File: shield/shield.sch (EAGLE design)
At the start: 13 parts, among them IC1 LM75, Q1 BUZ11BV, Q2 BUZ11BV, Q3 BUZ11BV, Q4 BUZ11BV, U1 TLC5925IDWR

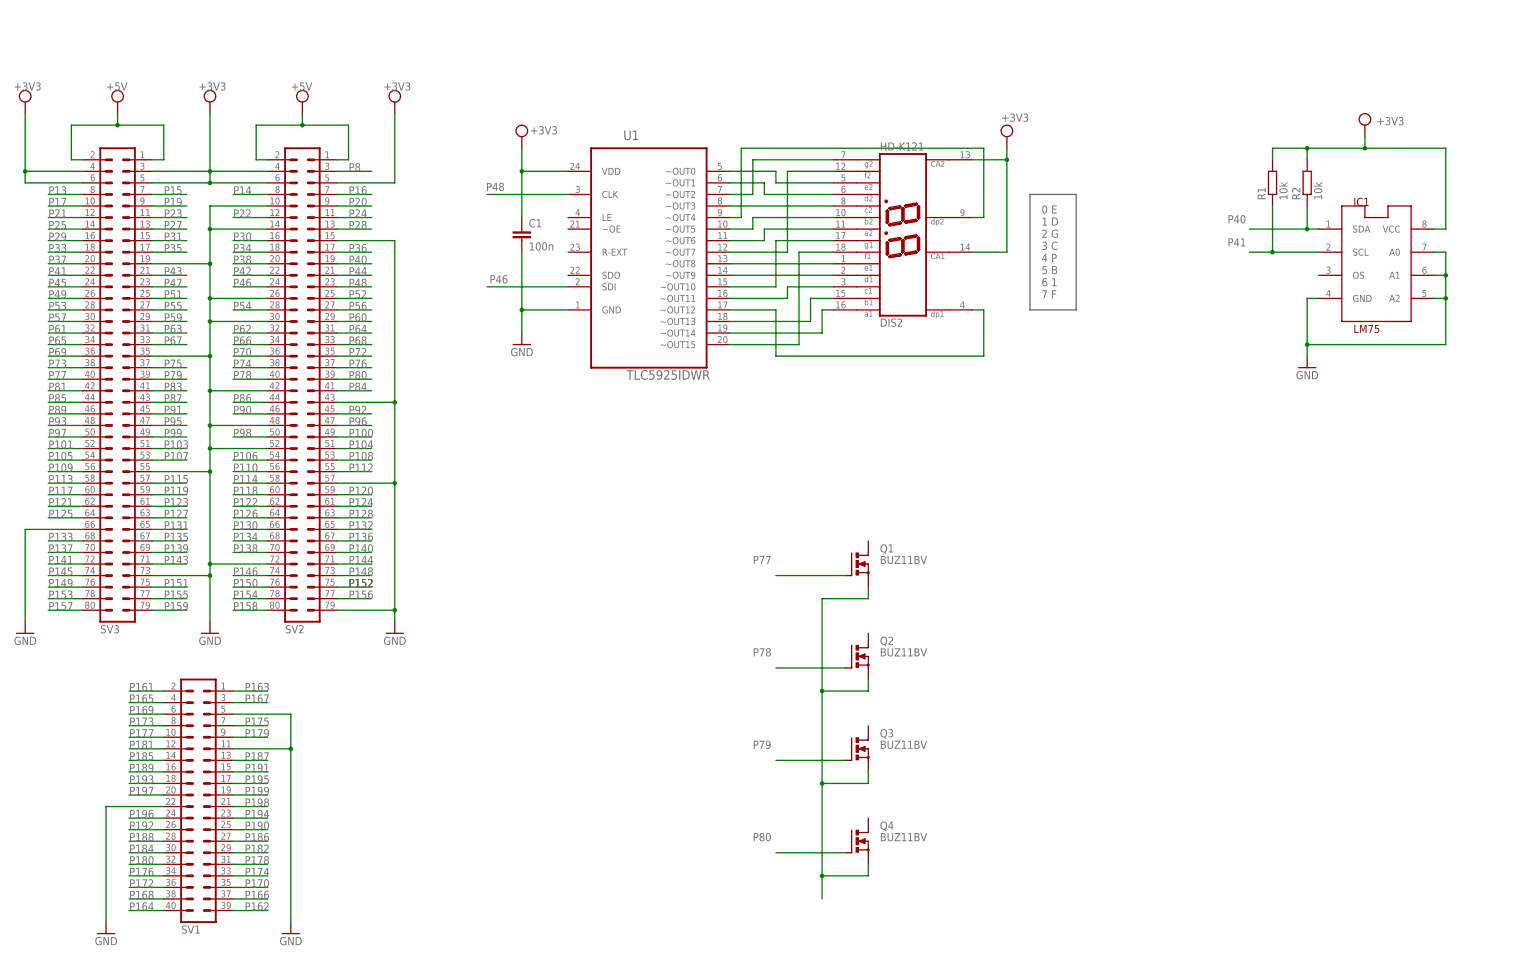
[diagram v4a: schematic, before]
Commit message: Update shield schematic and pcb
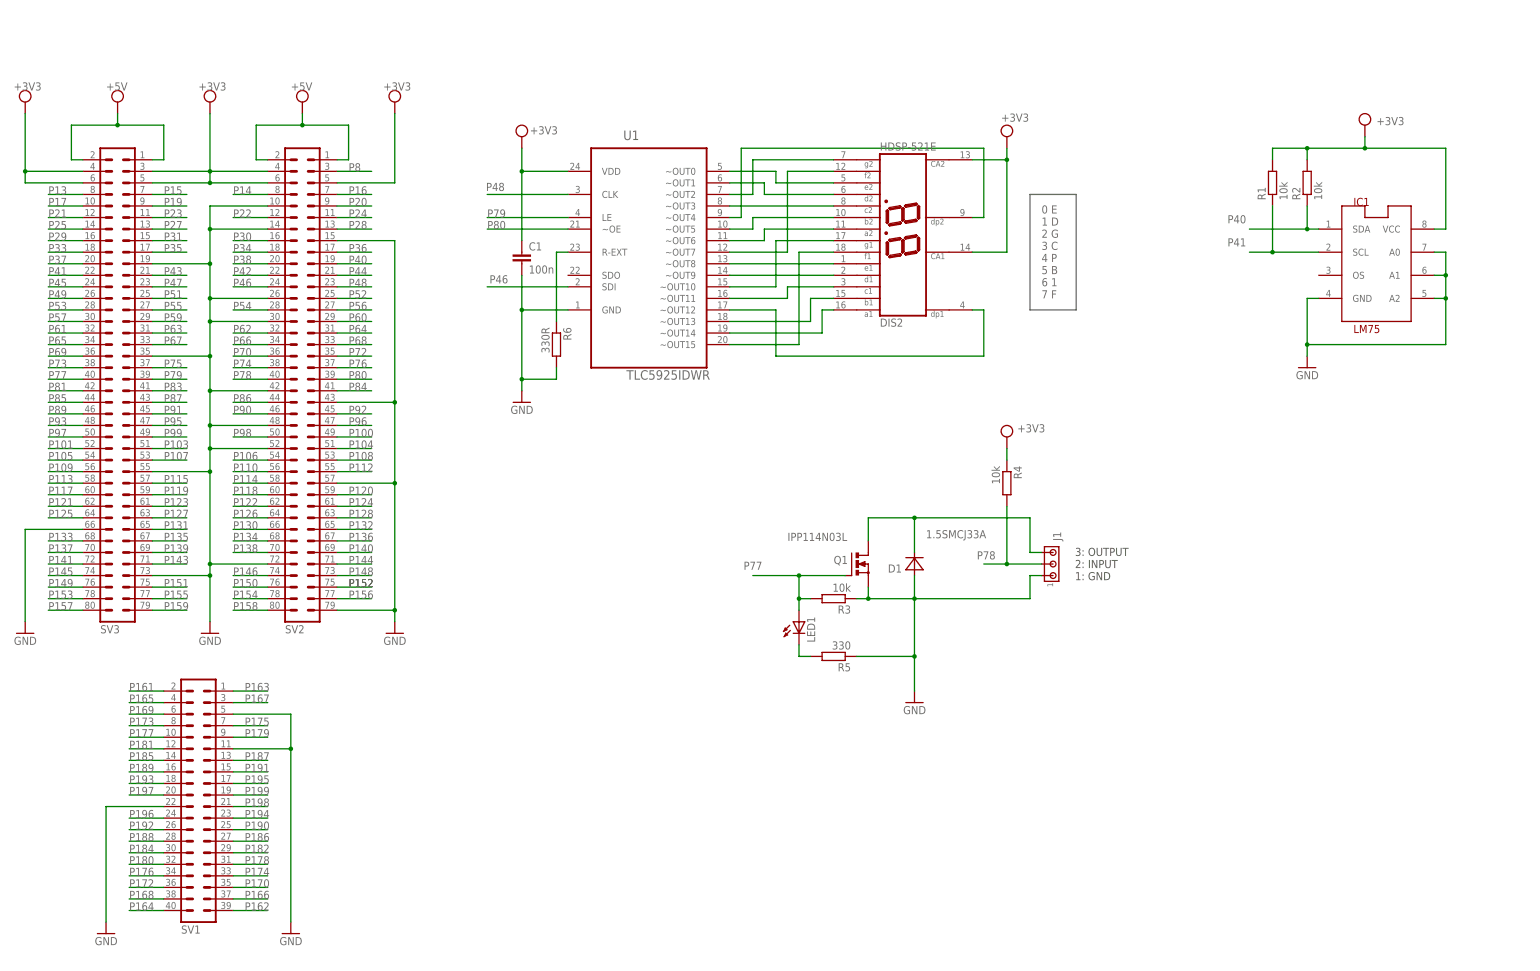
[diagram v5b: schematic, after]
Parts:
- removed Q2, Q3, Q4: BUZ11BV, transistor-power:BUZ11BV
- added D1: 1.5SMCJ33A, seb:MBRS340
- added J1: (no value), con-amp:MTA03-100
- added LED1: (no value), led:LED5MM
- added R3, R4: 10k, rcl:R-EU_0207/10
- added R5: 330, rcl:R-EU_0207/10
- added R6: 330R, rcl:R-EU_0207/10
- DIS2: value HD-K121 -> HDSP-521E
- Q1: value BUZ11BV -> IPP114N03L
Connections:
- new net N$18: LED1.C, R5.2
- new net N$20: R6.1, U1.R-EXT
- net +3V3: now also R4.1
- net GND: now also D1.A, J1.1, Q1.S, R3.1, R5.1, R6.2
- net N$17: now also D1.C, J1.3, Q1.D; no longer Q1.S, Q2.S, Q3.S, Q4.S
- net P77: now also LED1.A, R3.2
- net P78: now also J1.2, R4.2; no longer Q2.G
- net P79: now also U1.LE; no longer Q3.G
- net P80: now also U1.~OE; no longer Q4.G
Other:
- note added: "3: OUTPUT 2: INPUT 1: GND"
- moved on the sheet: C1

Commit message: Update board file
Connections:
- removed net +5V: SV2.1, SV2.2, SV3.1, SV3.2
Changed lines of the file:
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@@
 <part name="GND5" library="supply1" deviceset="GND" device=""/>
 <part name="SUPPLY2" library="supply2" deviceset="VDD" device="" value="VDD"/>
-<part name="SUPPLY1" library="supply2" deviceset="VDD" device=""/>
-<part name="SUPPLY3" library="supply2" deviceset="VDD" device=""/>
 <part name="SUPPLY4" library="supply2" deviceset="VDD" device="" value="VDD"/>
 <part name="SUPPLY5" library="supply2" deviceset="VDD" device="" value="VDD"/>
@@
 <instance part="GND5" gate="1" x="33.02" y="15.24" rot="MR0"/>
 <instance part="SUPPLY2" gate="G$1" x="-48.26" y="132.08" smashed="yes"/>
-<instance part="SUPPLY1" gate="G$1" x="-27.94" y="132.08" smashed="yes"/>
-<instance part="SUPPLY3" gate="G$1" x="12.7" y="132.08" smashed="yes"/>
 <instance part="SUPPLY4" gate="G$1" x="-7.62" y="132.08" smashed="yes"/>
 <instance part="SUPPLY5" gate="G$1" x="33.02" y="132.08" smashed="yes"/>
@@
 </segment>
 </net>
-<net name="+5V" class="0">
-<segment>
-<pinref part="SV3" gate="G$1" pin="2"/>
-<wire x1="-35.56" y1="119.38" x2="-38.1" y2="119.38" width="0.1524" layer="91"/>
-<wire x1="-38.1" y1="119.38" x2="-38.1" y2="127" width="0.1524" layer="91"/>
-<pinref part="SV3" gate="G$1" pin="1"/>
-<wire x1="-20.32" y1="119.38" x2="-17.78" y2="119.38" width="0.1524" layer="91"/>
-<wire x1="-17.78" y1="119.38" x2="-17.78" y2="127" width="0.1524" layer="91"/>
-<wire x1="-17.78" y1="127" x2="-27.94" y2="127" width="0.1524" layer="91"/>
-<pinref part="SUPPLY1" gate="G$1" pin="VDD"/>
-<wire x1="-27.94" y1="127" x2="-38.1" y2="127" width="0.1524" layer="91"/>
-<wire x1="-27.94" y1="127" x2="-27.94" y2="129.54" width="0.1524" layer="91"/>
-<label x="-30.48" y="134.62" size="1.778" layer="95"/>
-<junction x="-27.94" y="127"/>
-</segment>
-<segment>
-<wire x1="22.86" y1="119.38" x2="22.86" y2="127" width="0.1524" layer="91"/>
-<wire x1="20.32" y1="119.38" x2="22.86" y2="119.38" width="0.1524" layer="91"/>
-<pinref part="SV2" gate="G$1" pin="1"/>
-<pinref part="SV2" gate="G$1" pin="2"/>
-<wire x1="5.08" y1="119.38" x2="2.54" y2="119.38" width="0.1524" layer="91"/>
-<wire x1="2.54" y1="119.38" x2="2.54" y2="127" width="0.1524" layer="91"/>
-<wire x1="2.54" y1="127" x2="12.7" y2="127" width="0.1524" layer="91"/>
-<pinref part="SUPPLY3" gate="G$1" pin="VDD"/>
-<wire x1="12.7" y1="127" x2="22.86" y2="127" width="0.1524" layer="91"/>
-<wire x1="12.7" y1="129.54" x2="12.7" y2="127" width="0.1524" layer="91"/>
-<junction x="12.7" y="127"/>
-<label x="10.16" y="134.62" size="1.778" layer="95"/>
-</segment>
-</net>
 <net name="N$1" class="0">
 <segment>
@@
 </sheet>
 </sheets>
+<errors>
+</errors>
 </schematic>
 </drawing>

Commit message: Add capacitor
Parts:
- added C2: 100n, capacitor-wima:C2.5/2
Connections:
- net +3V3: now also C2.1
- net GND: now also C2.2
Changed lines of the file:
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@@
 <part name="R6" library="rcl" deviceset="R-EU_" device="0207/10" value="330R"/>
 <part name="D1" library="seb" deviceset="MBRS340" device="" value="1.5SMCJ33A"/>
+<part name="C2" library="capacitor-wima" deviceset="C" device="2.5/2" value="100n"/>
 </parts>
 <sheets>
@@
 <attribute name="VALUE" x="149.8346" y="36.1442" size="1.778" layer="96"/>
 </instance>
+<instance part="C2" gate="G$1" x="274.32" y="91.44"/>
 </instances>
 <busses>
@@
 <junction x="264.16" y="88.9"/>
 <junction x="233.68" y="78.74"/>
+<pinref part="C2" gate="G$1" pin="2"/>
+<wire x1="264.16" y1="78.74" x2="274.32" y2="78.74" width="0.1524" layer="91"/>
+<wire x1="274.32" y1="78.74" x2="274.32" y2="86.36" width="0.1524" layer="91"/>
+<junction x="264.16" y="78.74"/>
 </segment>
 <segment>
@@
 <wire x1="264.16" y1="104.14" x2="261.62" y2="104.14" width="0.1524" layer="91"/>
 <junction x="233.68" y="121.92"/>
-</segment>
-<segment>
+<pinref part="C2" gate="G$1" pin="1"/>
+<wire x1="264.16" y1="104.14" x2="274.32" y2="104.14" width="0.1524" layer="91"/>
+<wire x1="274.32" y1="104.14" x2="274.32" y2="93.98" width="0.1524" layer="91"/>
+<junction x="264.16" y="104.14"/>
+</segment>
+<segment>

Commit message: update shield
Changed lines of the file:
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@@
 <pinref part="U1" gate="A" pin="~OUT4"/>
 <wire x1="106.68" y1="106.68" x2="109.22" y2="106.68" width="0.1524" layer="91"/>
-<wire x1="109.22" y1="106.68" x2="109.22" y2="121.92" width="0.1524" layer="91"/>
-<wire x1="109.22" y1="121.92" x2="162.56" y2="121.92" width="0.1524" layer="91"/>
-<wire x1="162.56" y1="121.92" x2="162.56" y2="106.68" width="0.1524" layer="91"/>
+<wire x1="109.22" y1="106.68" x2="109.22" y2="124.46" width="0.1524" layer="91"/>
+<wire x1="109.22" y1="124.46" x2="162.56" y2="124.46" width="0.1524" layer="91"/>
+<wire x1="162.56" y1="124.46" x2="162.56" y2="106.68" width="0.1524" layer="91"/>
 <pinref part="DIS2" gate="R" pin="DP2"/>
 <wire x1="162.56" y1="106.68" x2="160.02" y2="106.68" width="0.1524" layer="91"/>
